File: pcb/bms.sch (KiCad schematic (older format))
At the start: 0 parts

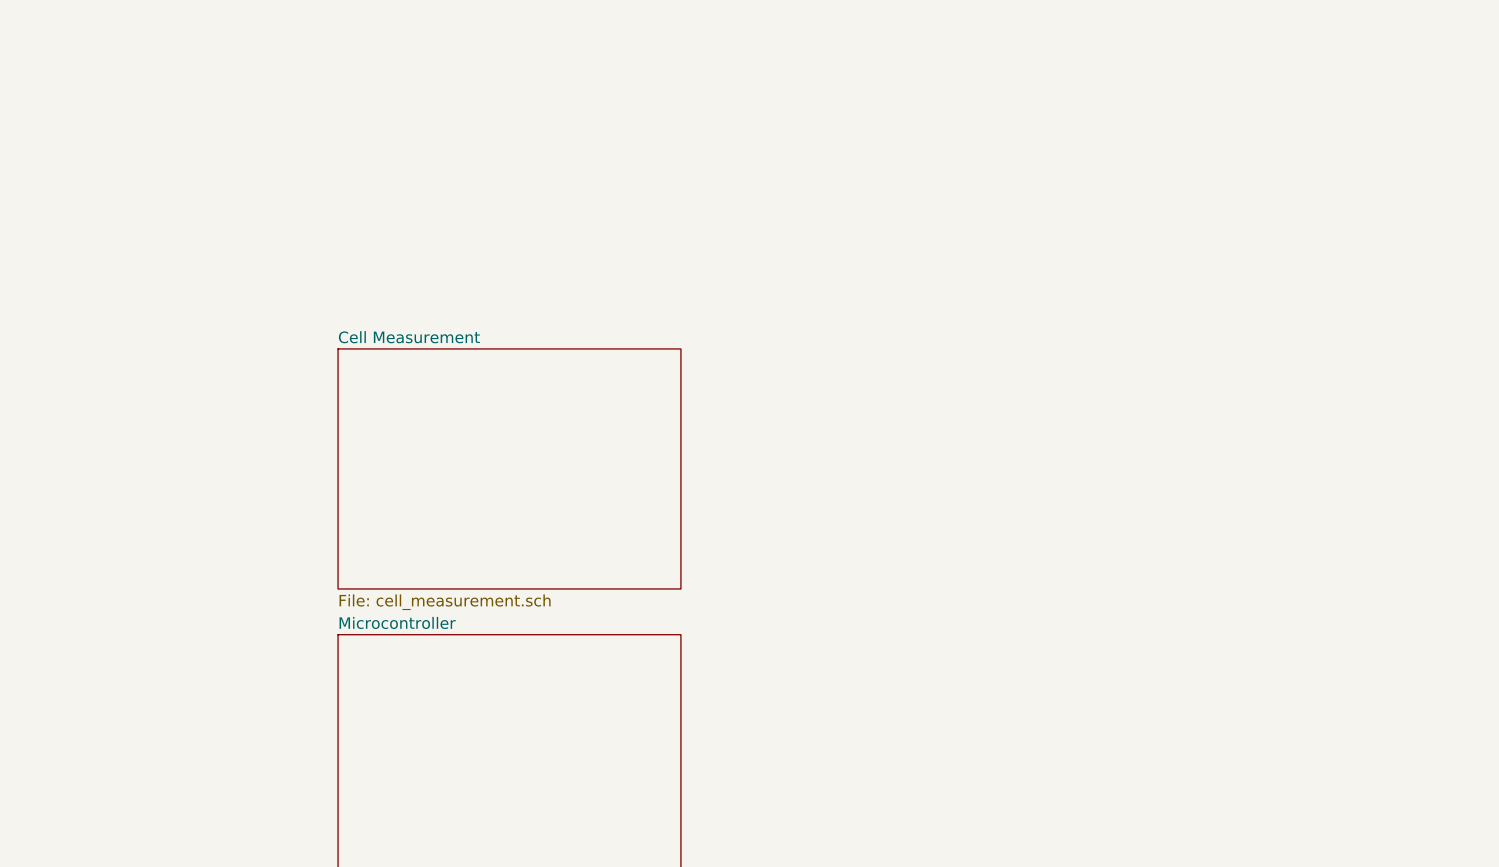
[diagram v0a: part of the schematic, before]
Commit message: finished cell tab board
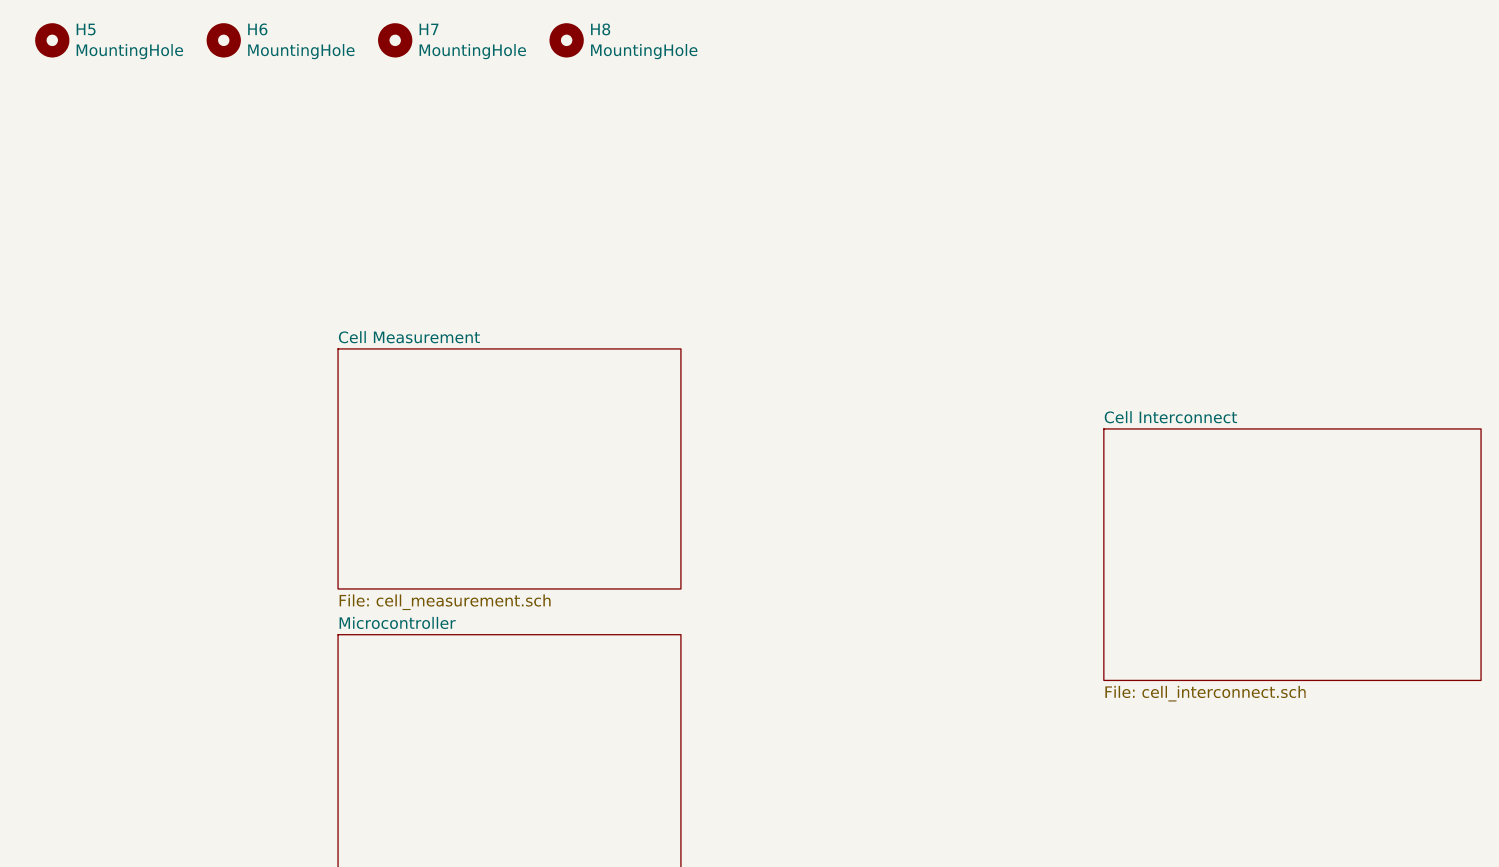
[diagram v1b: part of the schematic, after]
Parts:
- added H5, H6, H7, H8: MountingHole, MountingHole:MountingHole_3.2mm_M3, symbol Mechanical:MountingHole
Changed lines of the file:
@@
 $Descr A4 11693 8268
 encoding utf-8
-Sheet 1 3
+Sheet 1 4
 Title ""
 Date ""
@@
 F1 "microcontroller.sch" 50
 $EndSheet
+$Sheet
+S 5250 2350 1650 1100
+U 607E490C
+F0 "Cell Interconnect" 50
+F1 "cell_interconnect.sch" 50
+$EndSheet
+$Comp
+L Mechanical:MountingHole H?
+U 1 1 6082D249
+P 650 650
+AR Path="/607E490C/6082D249" Ref="H?"  Part="1"
+AR Path="/6082D249" Ref="H5"  Part="1"
+F 0 "H5" H 750 696 50  0000 L CNN
+F 1 "MountingHole" H 750 605 50  0000 L CNN
+F 2 "MountingHole:MountingHole_3.2mm_M3" H 650 650 50  0001 C CNN
+F 3 "~" H 650 650 50  0001 C CNN
+	1    650  650
+	1    0    0    -1
+$EndComp
+$Comp
+L Mechanical:MountingHole H?
+U 1 1 6082D24F
+P 1400 650
+AR Path="/607E490C/6082D24F" Ref="H?"  Part="1"
+AR Path="/6082D24F" Ref="H6"  Part="1"
+F 0 "H6" H 1500 696 50  0000 L CNN
+F 1 "MountingHole" H 1500 605 50  0000 L CNN
+F 2 "MountingHole:MountingHole_3.2mm_M3" H 1400 650 50  0001 C CNN
+F 3 "~" H 1400 650 50  0001 C CNN
+	1    1400 650
+	1    0    0    -1
+$EndComp
+$Comp
+L Mechanical:MountingHole H?
+U 1 1 6082D255
+P 2150 650
+AR Path="/607E490C/6082D255" Ref="H?"  Part="1"
+AR Path="/6082D255" Ref="H7"  Part="1"
+F 0 "H7" H 2250 696 50  0000 L CNN
+F 1 "MountingHole" H 2250 605 50  0000 L CNN
+F 2 "MountingHole:MountingHole_3.2mm_M3" H 2150 650 50  0001 C CNN
+F 3 "~" H 2150 650 50  0001 C CNN
+	1    2150 650
+	1    0    0    -1
+$EndComp
+$Comp
+L Mechanical:MountingHole H?
+U 1 1 6082D25B
+P 2900 650
+AR Path="/607E490C/6082D25B" Ref="H?"  Part="1"
+AR Path="/6082D25B" Ref="H8"  Part="1"
+F 0 "H8" H 3000 696 50  0000 L CNN
+F 1 "MountingHole" H 3000 605 50  0000 L CNN
+F 2 "MountingHole:MountingHole_3.2mm_M3" H 2900 650 50  0001 C CNN
+F 3 "~" H 2900 650 50  0001 C CNN
+	1    2900 650
+	1    0    0    -1
+$EndComp
 $EndSCHEMATC

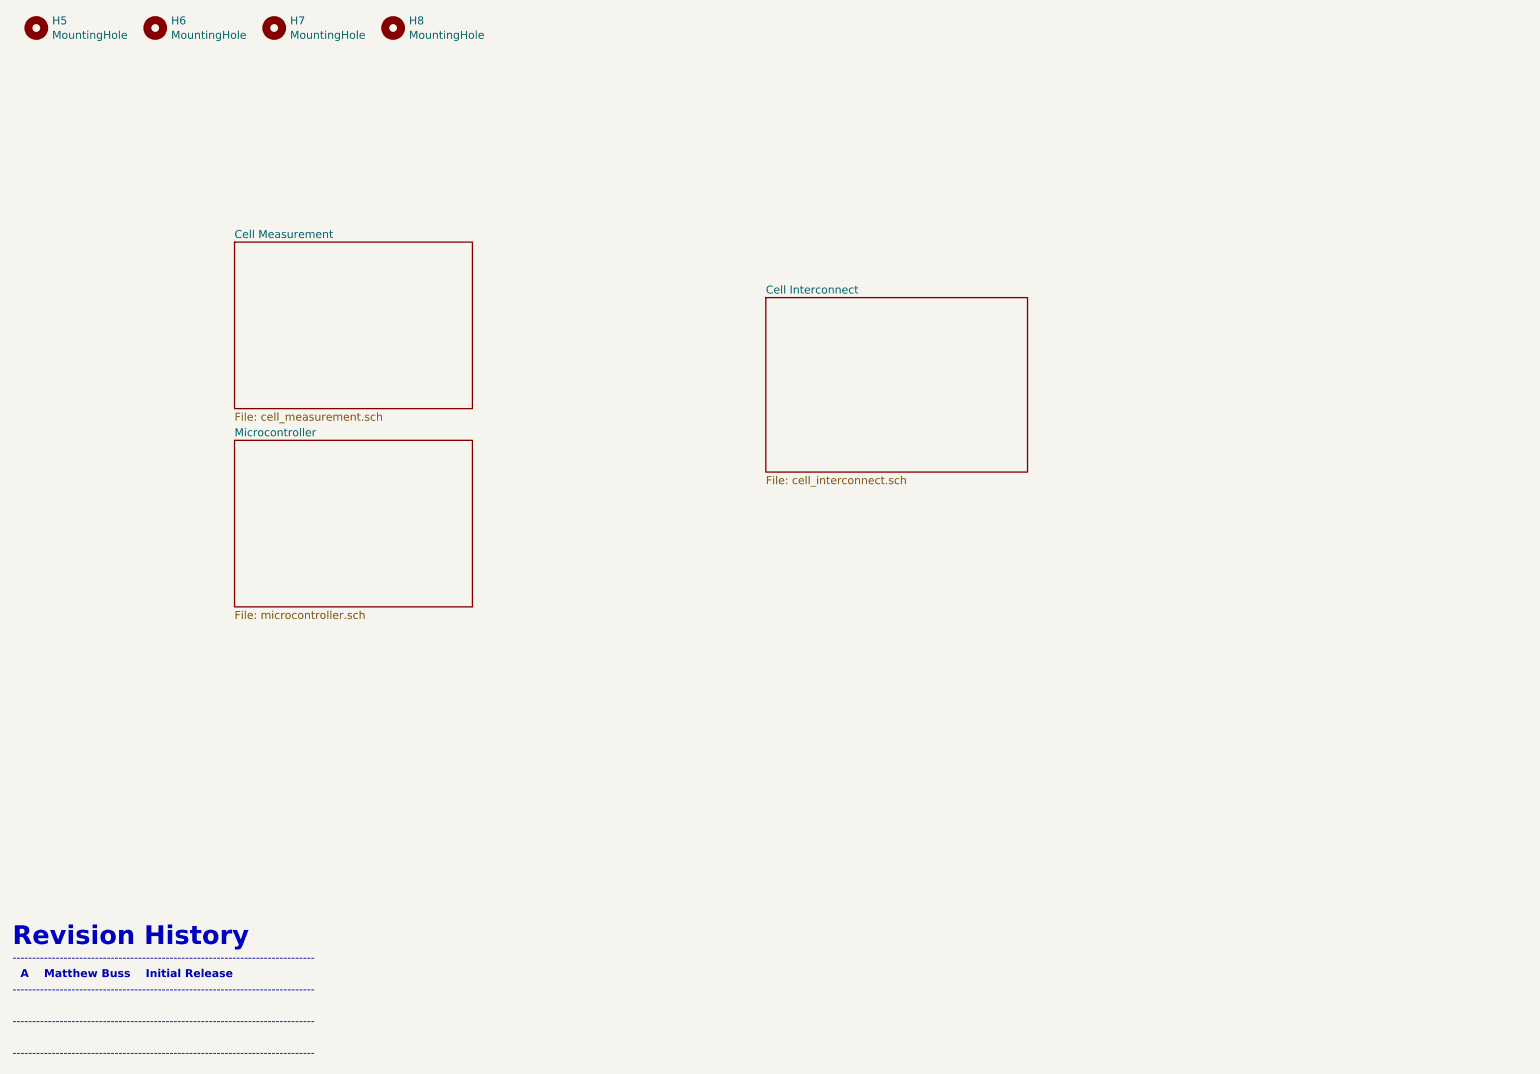
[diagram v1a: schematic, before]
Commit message: AFE mostly complete
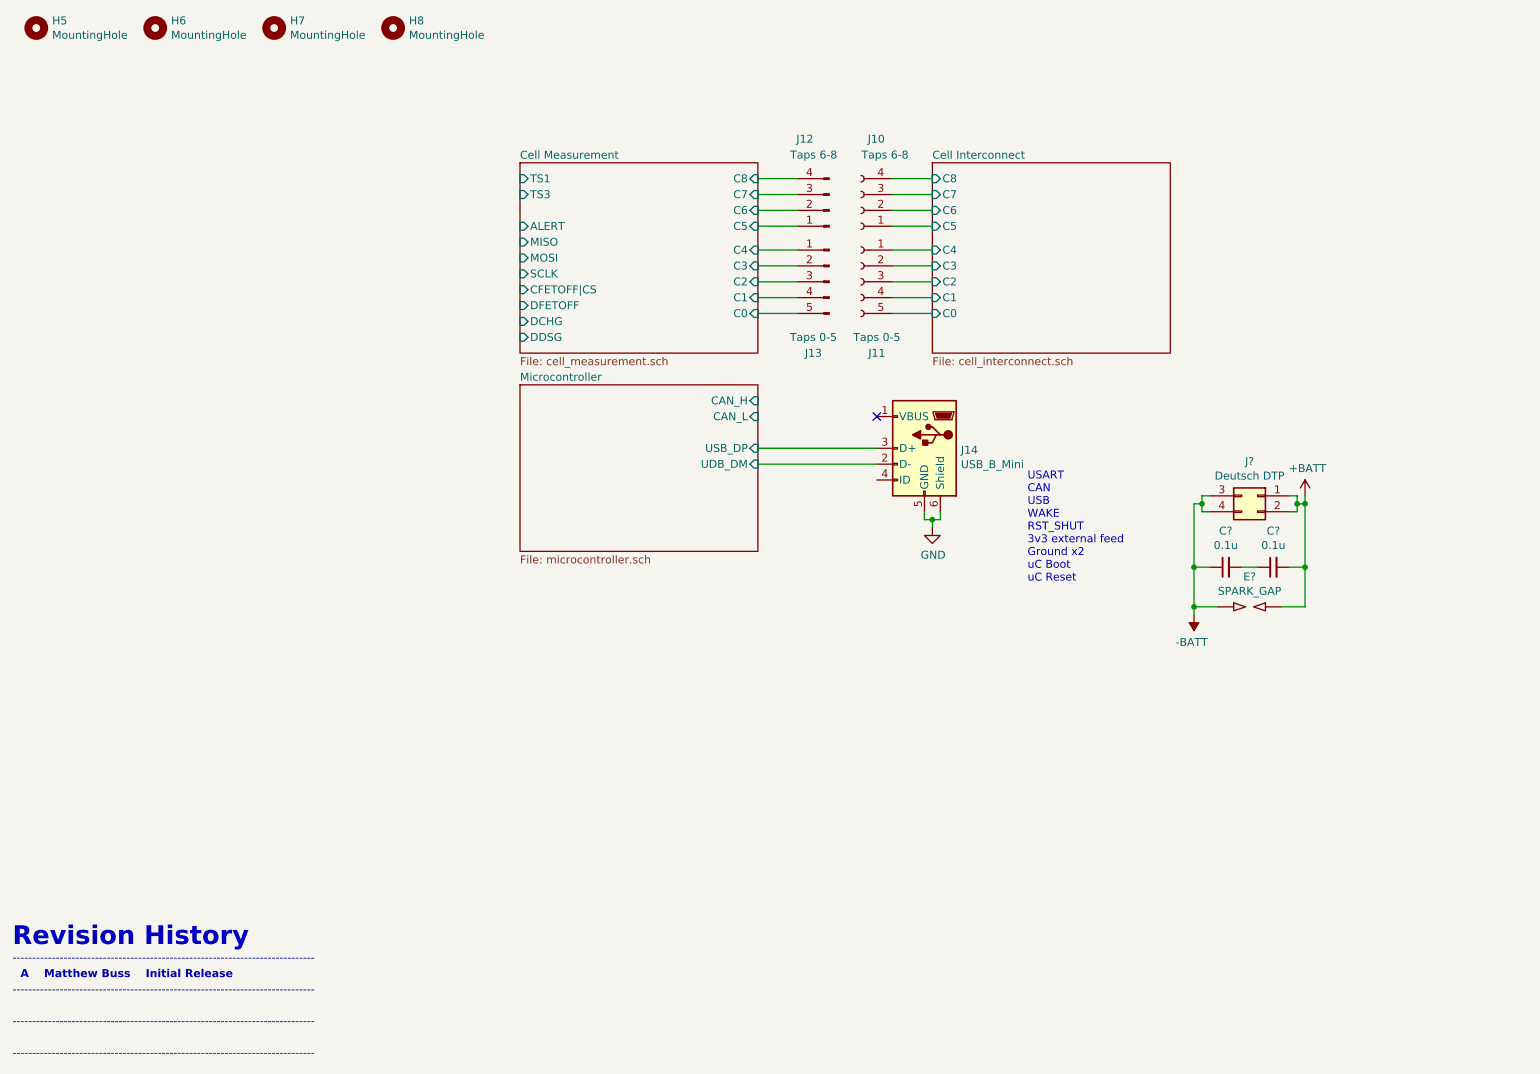
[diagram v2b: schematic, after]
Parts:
- added C? (x2): 0.1u, symbol Device:C_Small
- added E?: SPARK_GAP, symbol Device:SPARK_GAP
- added J10: Taps 6-8, Connector_PinSocket_2.54mm:PinSocket_1x04_P2.54mm_Vertical, symbol Connector:Conn_01x04_Female
- added J11: Taps 0-5, Connector_PinSocket_2.54mm:PinSocket_1x05_P2.54mm_Vertical, symbol Connector:Conn_01x05_Female
- added J12: Taps 6-8, Connector_PinHeader_2.54mm:PinHeader_1x04_P2.54mm_Vertical, symbol Connector:Conn_01x04_Male
- added J13: Taps 0-5, Connector_PinHeader_2.54mm:PinHeader_1x05_P2.54mm_Vertical, symbol Connector:Conn_01x05_Male
- added J14: USB_B_Mini, symbol Connector:USB_B_Mini
- added J?: Deutsch DTP, symbol Connector_Generic:Conn_02x02_Top_Bottom
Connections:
- new net: C?.1, C?.2
- new net +BATT: C?.2, E?.2, J?.1 (Pin_1), J?.2 (Pin_2)
- new net -BATT: C?.1, E?.1, J?.3 (Pin_3), J?.4 (Pin_4)
- new net Cell Interconnect/C0: J11.5 (Pin_5)
- new net Cell Interconnect/C1: J11.4 (Pin_4)
- new net Cell Interconnect/C2: J11.3 (Pin_3)
- new net Cell Interconnect/C3: J11.2 (Pin_2)
- new net Cell Interconnect/C4: J11.1 (Pin_1)
- new net Cell Interconnect/C5: J10.1 (Pin_1)
- new net Cell Interconnect/C6: J10.2 (Pin_2)
- new net Cell Interconnect/C7: J10.3 (Pin_3)
- new net Cell Interconnect/C8: J10.4 (Pin_4)
- new net Cell Measurement/C0: J13.5 (Pin_5)
- new net Cell Measurement/C1: J13.4 (Pin_4)
- new net Cell Measurement/C2: J13.3 (Pin_3)
- new net Cell Measurement/C3: J13.2 (Pin_2)
- new net Cell Measurement/C4: J13.1 (Pin_1)
- new net Cell Measurement/C5: J12.1 (Pin_1)
- new net Cell Measurement/C6: J12.2 (Pin_2)
- new net Cell Measurement/C7: J12.3 (Pin_3)
- new net Cell Measurement/C8: J12.4 (Pin_4)
- new net GND: J14.5 (GND), J14.6 (Shield)
- new net Microcontroller/UDB_DM: J14.2 (D-)
- new net Microcontroller/USB_DP: J14.3 (D+)
- no-connect marks 0 -> 1
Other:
- note added: "USART\nCAN\nUSB\nWAKE\nRST_SHUT\n3v3 external feed\nGround x2\nuC Boot\nuC Reset"

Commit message: connectors, microcontroller
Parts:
- added J?: Thermistor 1, symbol Connector:Conn_01x02_Female
- added J?: Thermistor 2, symbol Connector:Conn_01x02_Female
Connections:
- net Cell Measurement/TS1: now also J?.1 (Pin_1)
- net Cell Measurement/TS3: now also J?.1 (Pin_1)
- net GND: now also J?.2 (Pin_2), J?.2 (Pin_2)
- net Microcontroller/UDB_DM renamed Microcontroller/USB_DM
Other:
- moved on the sheet: C?, E?, J?
